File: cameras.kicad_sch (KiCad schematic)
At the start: 30 parts

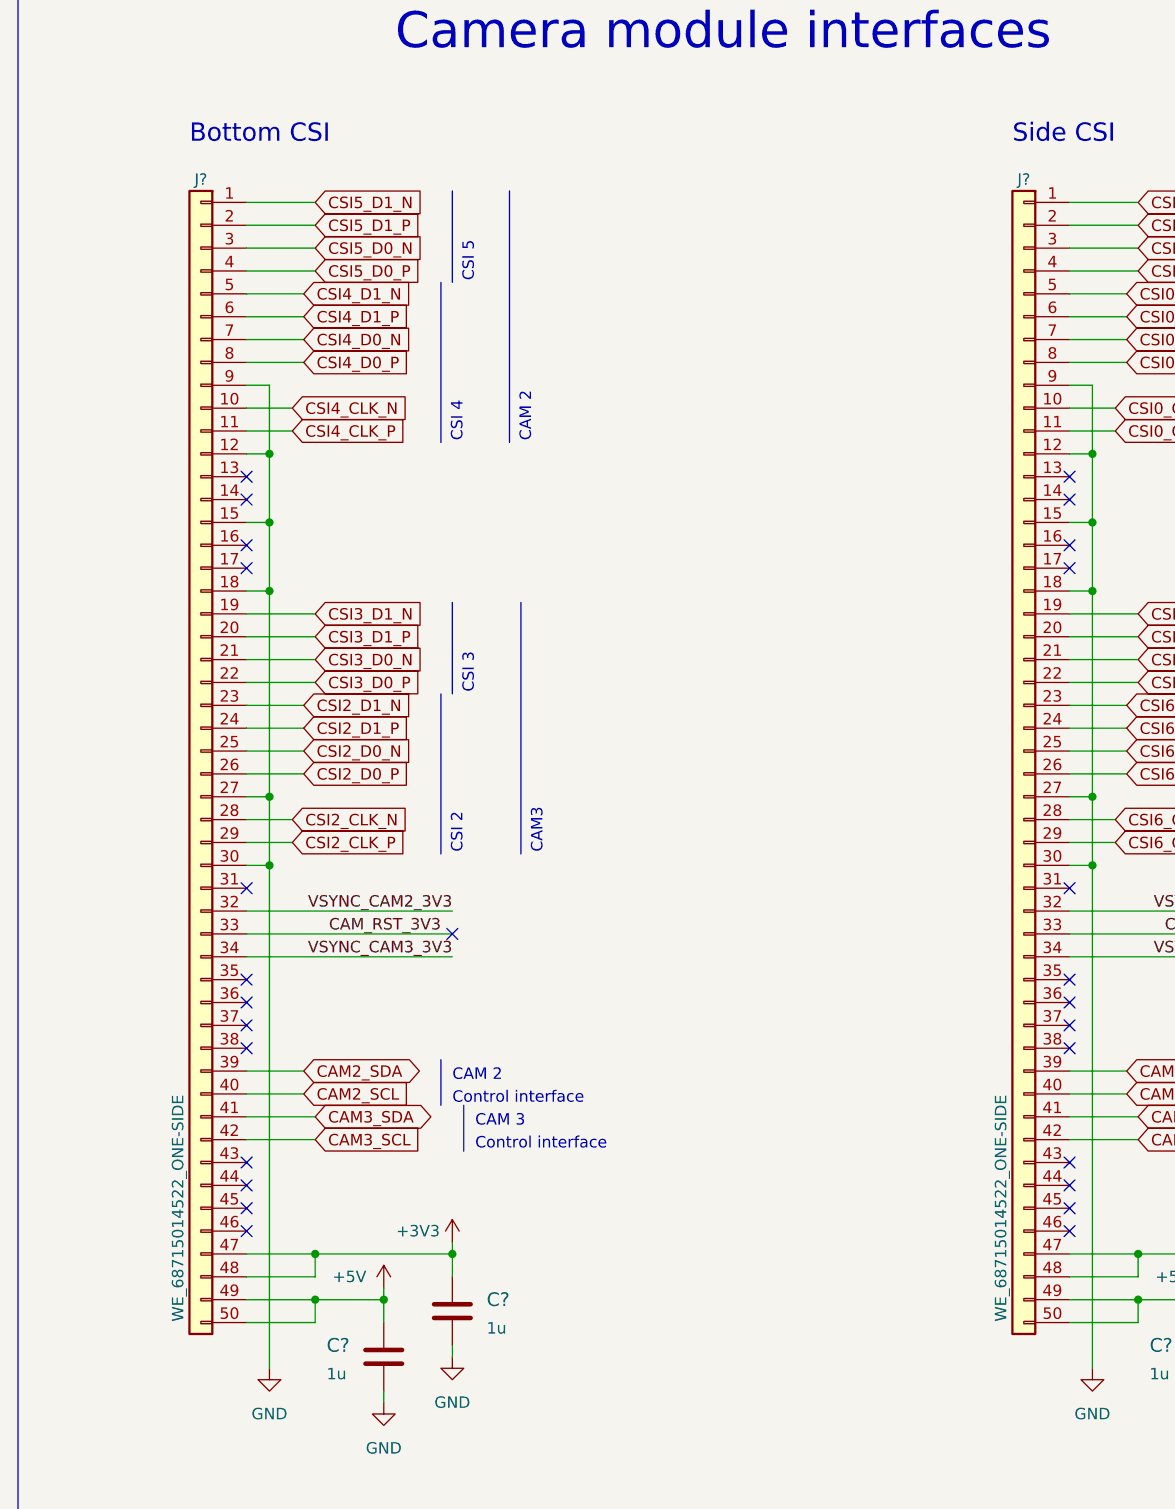
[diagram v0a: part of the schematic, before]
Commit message: Fixed adapter types
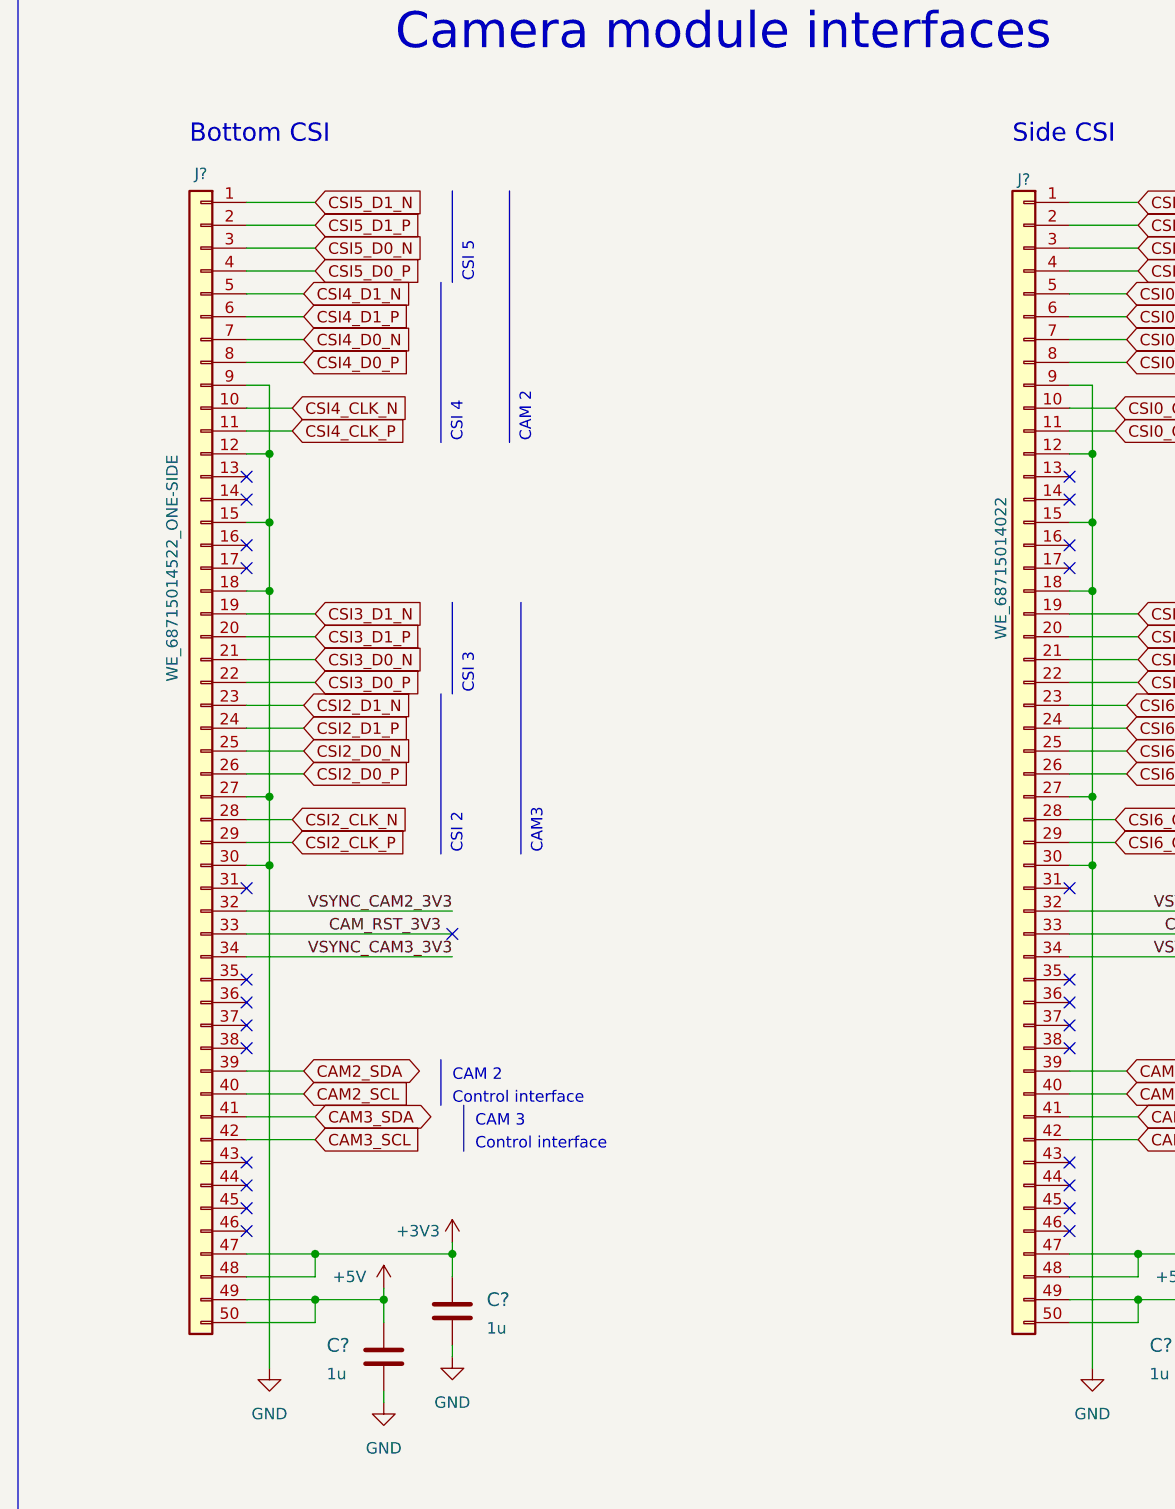
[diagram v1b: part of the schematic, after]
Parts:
- removed J? (x2): WE_68715014522_ONE-SIDE, antmicro-footprints:WE_68715014522_ONE-SIDE, symbol antmicroFCCConnectors:WE_68715014522_ONE-SIDE
- added J?: WE_68715014522_ONE-SIDE, antmicro-footprints:WE_68715014522_ONE-SIDE, symbol antmicroFCCConnectors:WE_68715014522_ONE-SIDE
- added J?: WE_68715014022, antmicro-footprints:WE_68715014022, symbol antmicroFCCConnectors:WE_68715014022
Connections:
- net +3V3: now also J?.47 (Pin_47), J?.47 (Pin_47), J?.48 (Pin_48), J?.48 (Pin_48)
- net +5V: now also J?.49 (Pin_49), J?.49 (Pin_49), J?.50 (Pin_50), J?.50 (Pin_50)
- net CAM0_SCL: now also J?.40 (Pin_40)
- net CAM0_SDA: now also J?.39 (Pin_39)
- net CAM1_RST_3V3: now also J?.33 (Pin_33)
- net CAM1_SCL: now also J?.42 (Pin_42)
- net CAM1_SDA: now also J?.41 (Pin_41)
- net CAM2_SCL: now also J?.40 (Pin_40)
- net CAM2_SDA: now also J?.39 (Pin_39)
- net CAM3_SCL: now also J?.42 (Pin_42)
- net CAM3_SDA: now also J?.41 (Pin_41)
- net CAM_RST_3V3: now also J?.33 (Pin_33)
- net CSI0_CLK_N: now also J?.10 (Pin_10)
- net CSI0_CLK_P: now also J?.11 (Pin_11)
- net CSI0_D0_N: now also J?.7 (Pin_7)
- net CSI0_D0_P: now also J?.8 (Pin_8)
- net CSI0_D1_N: now also J?.5 (Pin_5)
- net CSI0_D1_P: now also J?.6 (Pin_6)
- net CSI1_D0_N: now also J?.3 (Pin_3)
- net CSI1_D0_P: now also J?.4 (Pin_4)
- net CSI1_D1_N: now also J?.1 (Pin_1)
- net CSI1_D1_P: now also J?.2 (Pin_2)
- net CSI2_CLK_N: now also J?.28 (Pin_28)
- net CSI2_CLK_P: now also J?.29 (Pin_29)
- net CSI2_D0_N: now also J?.25 (Pin_25)
- net CSI2_D0_P: now also J?.26 (Pin_26)
- net CSI2_D1_N: now also J?.23 (Pin_23)
- net CSI2_D1_P: now also J?.24 (Pin_24)
- net CSI3_D0_N: now also J?.21 (Pin_21)
- net CSI3_D0_P: now also J?.22 (Pin_22)
- net CSI3_D1_N: now also J?.19 (Pin_19)
- net CSI3_D1_P: now also J?.20 (Pin_20)
- net CSI4_CLK_N: now also J?.10 (Pin_10)
- net CSI4_CLK_P: now also J?.11 (Pin_11)
- net CSI4_D0_N: now also J?.7 (Pin_7)
- net CSI4_D0_P: now also J?.8 (Pin_8)
- net CSI4_D1_N: now also J?.5 (Pin_5)
- net CSI4_D1_P: now also J?.6 (Pin_6)
- net CSI5_D0_N: now also J?.3 (Pin_3)
- net CSI5_D0_P: now also J?.4 (Pin_4)
- net CSI5_D1_N: now also J?.1 (Pin_1)
- net CSI5_D1_P: now also J?.2 (Pin_2)
- net CSI6_CLK_N: now also J?.28 (Pin_28)
- net CSI6_CLK_P: now also J?.29 (Pin_29)
- net CSI6_D0_N: now also J?.25 (Pin_25)
- net CSI6_D0_P: now also J?.26 (Pin_26)
- net CSI6_D1_N: now also J?.23 (Pin_23)
- net CSI6_D1_P: now also J?.24 (Pin_24)
- net CSI7_D0_N: now also J?.21 (Pin_21)
- net CSI7_D0_P: now also J?.22 (Pin_22)
- net CSI7_D1_N: now also J?.19 (Pin_19)
- net CSI7_D1_P: now also J?.20 (Pin_20)
- net GND: now also J?.12 (Pin_12), J?.12 (Pin_12), J?.15 (Pin_15), J?.15 (Pin_15), J?.18 (Pin_18), J?.18 (Pin_18), J?.27 (Pin_27), J?.27 (Pin_27), J?.30 (Pin_30), J?.30 (Pin_30), J?.9 (Pin_9), J?.9 (Pin_9)
- net VSYNC_CAM0_3V3: now also J?.32 (Pin_32)
- net VSYNC_CAM1_3V3: now also J?.34 (Pin_34)
- net VSYNC_CAM2_3V3: now also J?.32 (Pin_32)
- net VSYNC_CAM3_3V3: now also J?.34 (Pin_34)

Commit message: Fixes suggested in review
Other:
- moved on the sheet: J?
